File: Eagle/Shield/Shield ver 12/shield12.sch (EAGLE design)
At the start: 17 parts, among them J2 AVR_SPI_PROG_5X2_NEWPTH2, J3 AVR_SPI_PROG_5X2_NEWPTH2, J4 AVR_SPI_PROG_5X2_NEWPTH2, J5 AVR_SPI_PROG_5X2_NEWPTH2, J6 AVR_SPI_PROG_5X2_NEWPTH2, J7 AVR_SPI_PROG_5X2_NEWPTH2, J8 AVR_SPI_PROG_5X2_NEWPTH2, J9 AVR_SPI_PROG_5X2_NEWPTH2

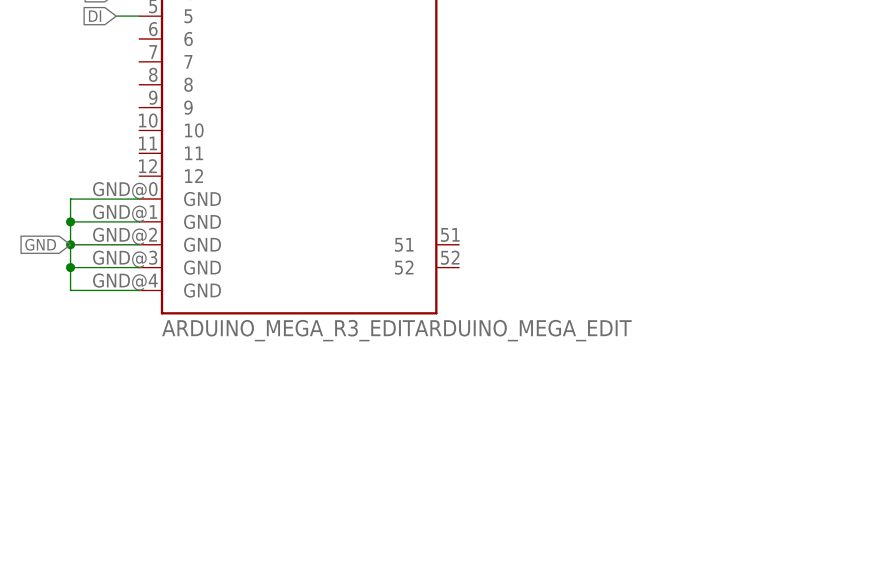
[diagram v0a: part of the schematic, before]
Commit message: Added pins 51 and 52 to use SPI for LEDS, re ran gerbers. The code now outputs to the LEDS over SPI and edits were made so that the strip is only outputted once
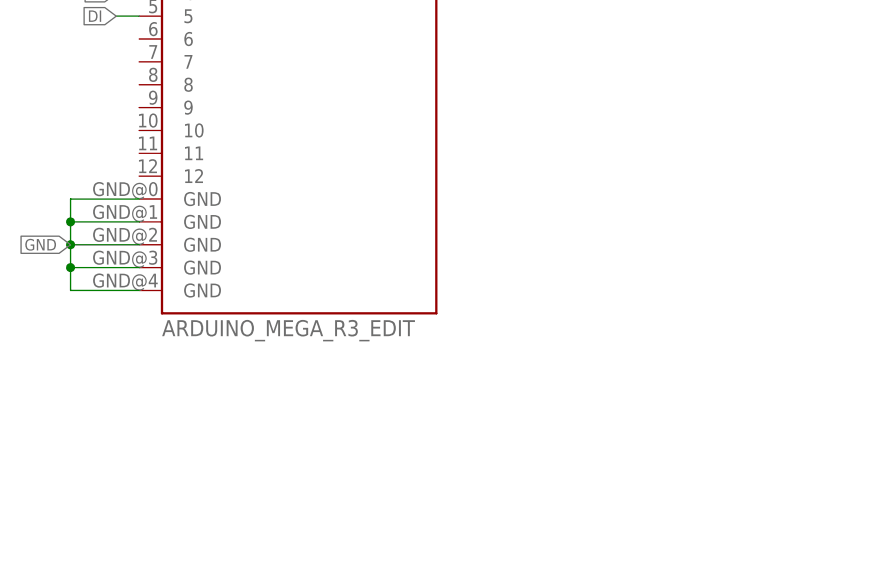
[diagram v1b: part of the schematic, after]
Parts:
- B2: value ARDUINO_MEGA_R3_EDITARDUINO_MEGA_EDIT -> ARDUINO_MEGA_R3_EDIT; device SparkFun-Boards:ARDUINO_MEGA_R3_EDITARDUINO_MEGA_EDIT -> SparkFun-Boards:ARDUINO_MEGA_R3_EDIT
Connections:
- net N$2: now also R1.2, R1.4, R1.6, R1.8, R2.1, R2.3, R2.5, R2.7
- net OUT: now also R2.2, R2.4, R2.6, R2.8
